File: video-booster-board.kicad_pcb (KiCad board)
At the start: 4 copper layers, 39 x 41.5 mm, 140 parts, among them IC1 INA180A1IDBVT, J1 0473460001, J10 M20-9990246, J11 MC-HVT1-S04-G, J12 solder_jumper, J13 solder_jumper, J14 solder_jumper, J2 CHDMI-AMSS-01-C-Vertical, J3 CHDMI-AMSS-01-C-Vertical, J4 694103107102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

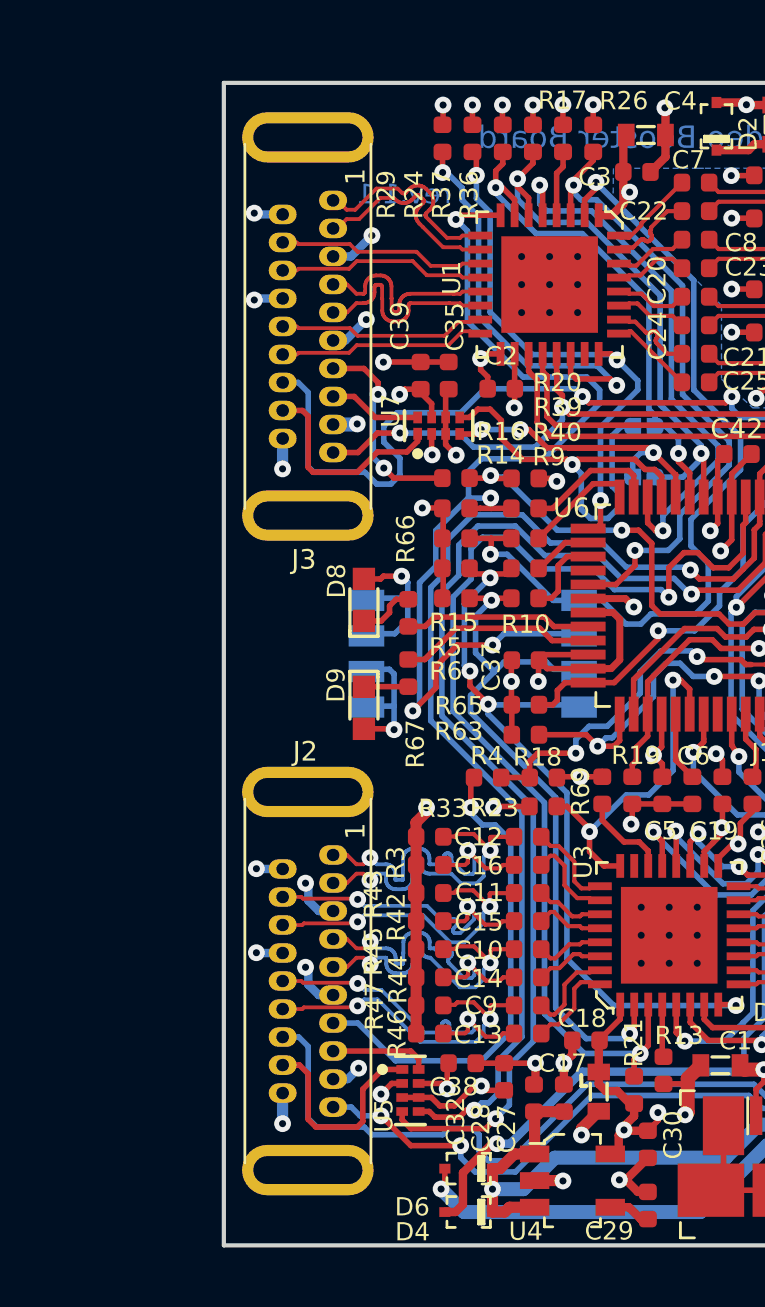
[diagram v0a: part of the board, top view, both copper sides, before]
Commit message: Restored plating on HDMI angular connectors
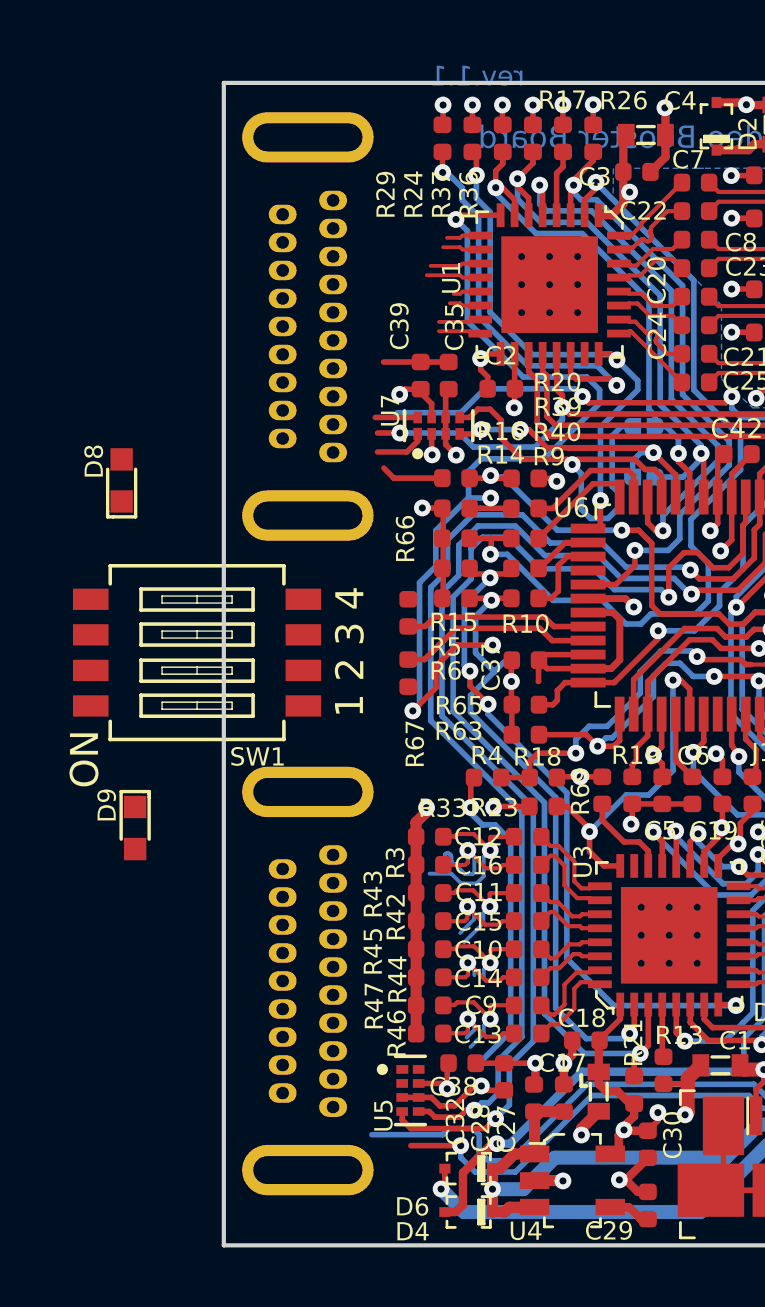
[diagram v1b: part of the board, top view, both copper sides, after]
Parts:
- J2, J3: moved to B.Cu
- SW1: value 1571983-5 -> VAL**; moved to F.Cu
- moved SW1 9.84 mm to (110.0, 78.8), turned to 90 degrees
- moved D8 9.64 mm to (107.4, 72.7)
- moved D9 9.22 mm to (107.8, 85.1)
- turned J2 to 270 degrees
- turned J3 to 270 degrees
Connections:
- J2 pad 12: GND -> /TX_IN_CLK_N
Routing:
- net GND: track 107.7 -> 82.7 mm, vias 58 -> 44
- net /RX_UTILITY: track 34.7 -> 24.6 mm
- net /TX_IN_D0_P: track 12.3 -> 4.21 mm, vias 2 -> 1
- net /TX_IN_D0_N: track 12.1 -> 4.09 mm, vias 2 -> 1
- net /TX_IN_CLK_P: track 12.5 -> 4.63 mm, vias 2 -> 1
- net /TX_SRC_SDA: track 7.66 -> 0.00 mm
- net /TX_IN_CLK_N: track 12.2 -> 4.77 mm, vias 2 -> 1
- net /TX_IN_D1_P: track 12.0 -> 4.66 mm, vias 2 -> 1
- net /TX_IN_D1_N: track 12.3 -> 5.24 mm, vias 2 -> 1
- net /RX_OUT_D0_P: track 7.45 -> 0.98 mm
- net /RX_OUT_D0_N: track 7.45 -> 1.12 mm
- net /TX_IN_D2_P: track 12.2 -> 5.90 mm, vias 2 -> 1
- net /RX_OUT_D2_P: track 7.44 -> 1.22 mm
- net /TX_UTILITY: track 36.8 -> 30.7 mm
- net Net-(J2-Pad13): track 17.6 -> 11.4 mm
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
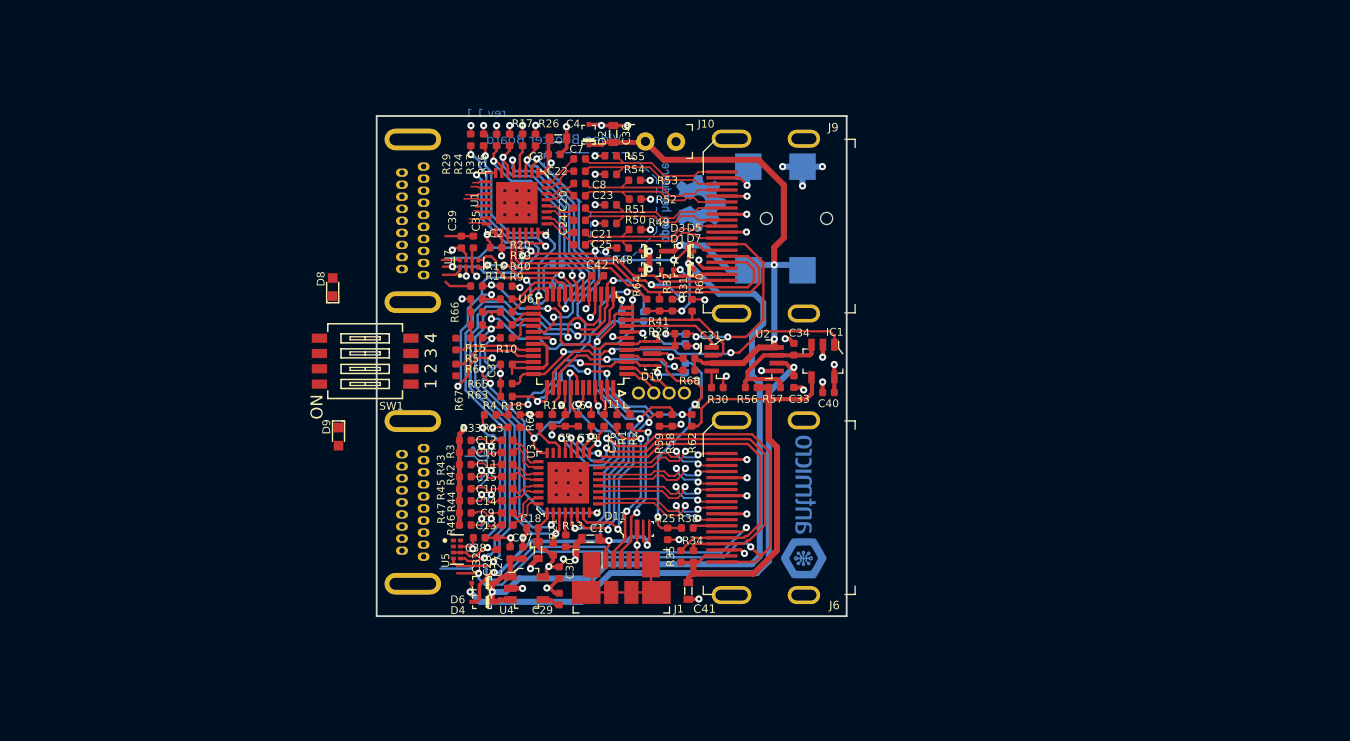
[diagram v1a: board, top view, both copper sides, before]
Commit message: Changed TX/RX side of PCB layout
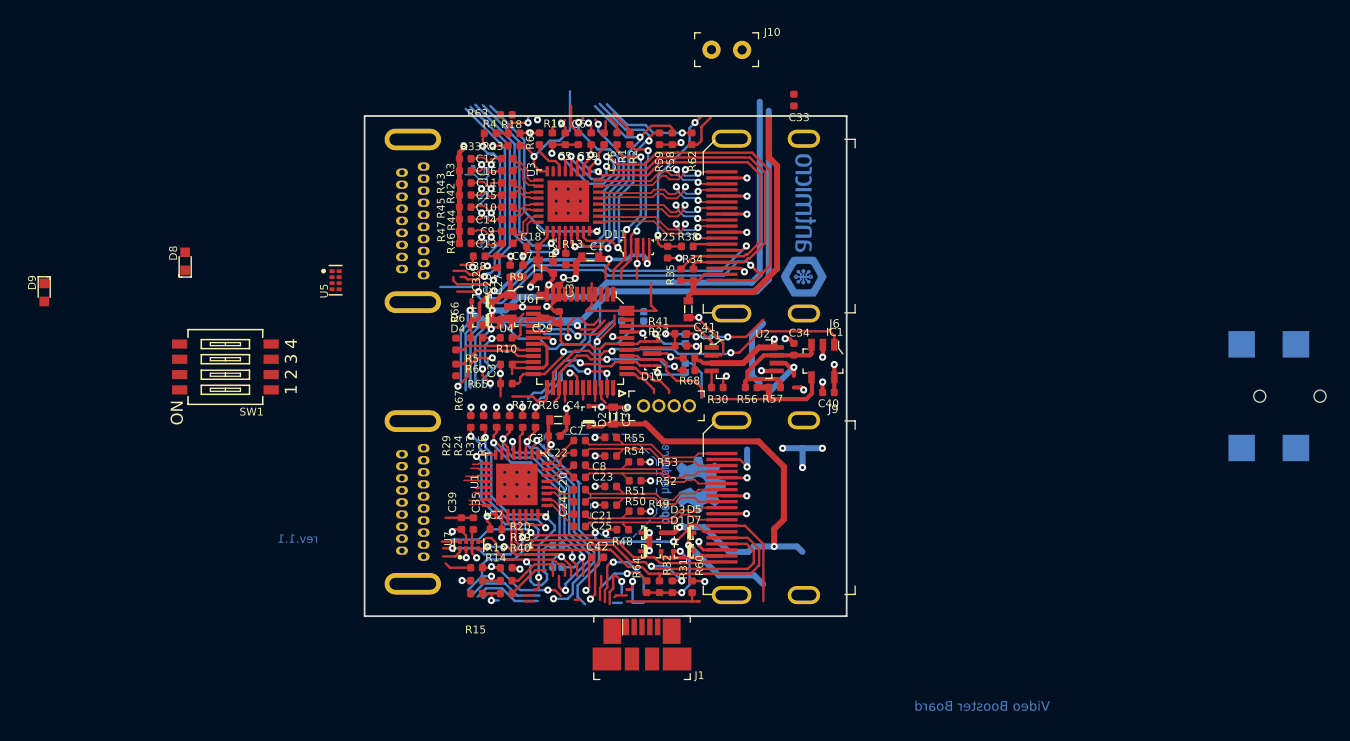
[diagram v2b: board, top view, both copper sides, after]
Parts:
- moved J4 43.5 mm to (190.8, 81.7)
- moved D9 27.2 mm to (83.4, 73.1)
- moved U5 24.5 mm to (107.6, 72.1)
- moved C11 23.4 mm to (121.8, 64.1)
- moved C15 23.4 mm to (121.8, 65.1)
- moved C16 23.4 mm to (121.8, 63.0)
- moved C17 23.4 mm to (124.4, 71.1)
- moved C18 23.4 mm to (123.9, 69.3)
- moved C20 23.4 mm to (127.8, 89.5)
- moved C21 23.4 mm to (127.8, 91.5)
- moved C22 23.4 mm to (127.8, 86.4)
- moved C25 23.4 mm to (127.8, 92.6)
- moved C27 23.4 mm to (123.1, 71.4)
- moved C28 23.4 mm to (122.1, 71.4)
- moved C32 23.4 mm to (121.0, 70.6)
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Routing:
- net /TX_DDET: track 39.5 -> 31.1 mm, vias 2 -> 1
- net +5V: track 62.0 -> 68.7 mm, vias 2 -> 3
- net +5VA: track 52.7 -> 46.6 mm
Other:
- board size 39 x 41.5 mm -> 40 x 41.5 mm

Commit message: Routing in progress
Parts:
- moved J10 51.7 mm to (134.7, 104.5)
- moved J1 44.1 mm to (132.6, 59.5), turned to 0 degrees
- moved C33 35.1 mm to (111.0, 62.9)
- moved C26 34.0 mm to (102.3, 80.3)
- moved D11 31.2 mm to (102.0, 63.4)
- moved C1 30.8 mm to (157.1, 82.1)
- moved C36 27.3 mm to (157.1, 90.2)
- moved U4 26.3 mm to (100.2, 86.5)
- moved D2 24.8 mm to (153.3, 85.4)
- moved R63 24.0 mm to (99.9, 68.5)
- moved R9 23.0 mm to (98.8, 73.9)
- moved R2 22.8 mm to (130.8, 83.1)
- moved R1 22.8 mm to (129.9, 83.1)
- moved C5 22.5 mm to (126.6, 82.9)
- moved C6 22.5 mm to (127.7, 82.9)
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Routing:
- net +5V: track 68.7 -> 2.96 mm, vias 3 -> 0
- net /TX_SRC_SCL_3V: track 45.6 -> 2.03 mm, vias 3 -> 1
- net /TX_SRC_SDA_3V: track 43.6 -> 2.96 mm, vias 3 -> 1
- net /VUSB: track 39.6 -> 1.11 mm, vias 4 -> 0
- net /RX_EQ0: track 33.7 -> 1.49 mm, vias 4 -> 0
- net +5VA: track 46.6 -> 19.3 mm, vias 3 -> 2
- net /TX_HPD: track 64.1 -> 39.0 mm, vias 4 -> 3
- net GND: track 82.7 -> 58.3 mm, vias 44 -> 33
- net /TX_UTILITY: track 30.7 -> 53.7 mm, vias 1 -> 2
- net /TX_SINK_SCL_3V: track 31.7 -> 9.69 mm, vias 3 -> 1
- net /TX_SRC_5V: track 48.8 -> 26.9 mm, vias 3 -> 1
- net /TX_IN_CLK_P: track 4.63 -> 25.4 mm
- net /TX_IN_D1_N: track 5.24 -> 25.8 mm
- net /TX_DDET: track 31.1 -> 11.0 mm, vias 1 -> 2
- net /TX_SINK_SDA_3V: track 32.9 -> 13.2 mm, vias 3 -> 2
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
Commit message: Routing II
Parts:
- SW1: value VAL** -> 1571983-5
- moved C1 28.8 mm to (128.4, 84.3)
- moved R9 23.0 mm to (121.8, 73.9)
- moved C4 20.2 mm to (105.9, 85.7)
- moved R39 18.1 mm to (122.3, 79.0), turned to 90 degrees
- moved R5 18.0 mm to (120.8, 76.9), turned to 180 degrees
- moved R10 17.8 mm to (121.8, 74.8)
- moved R14 17.7 mm to (120.8, 79.5), turned to 180 degrees
- moved R15 17.5 mm to (120.8, 80.7), turned to 180 degrees
- moved U7 17.3 mm to (117.8, 86.0)
- moved R40 16.5 mm to (120.8, 81.7)
- moved R6 16.0 mm to (120.8, 78.2), turned to 180 degrees
- moved J8 12.5 mm to (122.1, 84.1), turned to 180 degrees
- moved J12 11.5 mm to (120.4, 84.1), turned to 180 degrees
- moved R29 11.4 mm to (122.8, 72.9), turned to 0 degrees
- moved U5 11.3 mm to (118.8, 73.8), turned to 90 degrees
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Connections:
- J2 pad 11: (no net) -> GND
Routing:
- net /TX_HIZ_EN: track 3.99 -> 32.2 mm, vias 0 -> 2
- net /RX_EQ0: track 1.49 -> 13.2 mm, vias 0 -> 2
- net /RX_HIZ_EN: track 19.2 -> 29.5 mm, vias 3 -> 2
- net /RX_SINK_SDA_3V: track 9.31 -> 19.6 mm, vias 1 -> 3
- net /RX_EQ1_R: track 3.58 -> 13.3 mm, vias 0 -> 2
- net /RX_DCC_EN: track 14.9 -> 6.04 mm
- net /RX_SINK_CEC: track 14.5 -> 7.78 mm, vias 3 -> 1
- net GND: track 58.3 -> 64.7 mm, vias 33 -> 38
- net /RX_SINK_SCL_3V: track 11.2 -> 17.3 mm, vias 1 -> 3
- net /RX_UTILITY: track 22.4 -> 17.2 mm, vias 3 -> 2
- net /RX_SRC_SCL_3V: track 17.9 -> 22.8 mm
- net /TX_EQ1: track 11.4 -> 16.4 mm, vias 1 -> 3
- net /ADC5: track 5.15 -> 0.28 mm, vias 1 -> 0
- net /TX_EQ0: track 16.2 -> 20.8 mm, vias 1 -> 3
- net /TX_HPD_3V: track 13.2 -> 17.4 mm, vias 1 -> 2
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
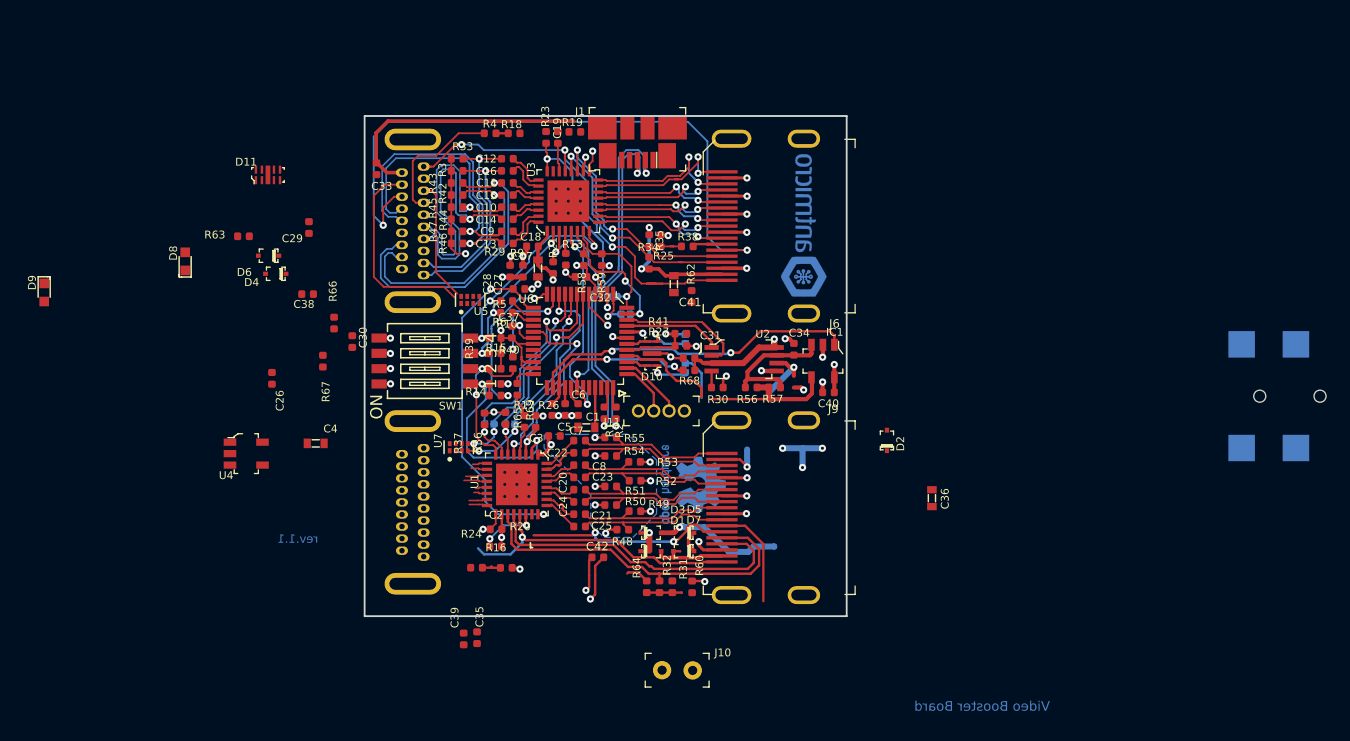
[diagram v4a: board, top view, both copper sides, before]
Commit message: SWD changed from pinhead to testpads, routing in progress
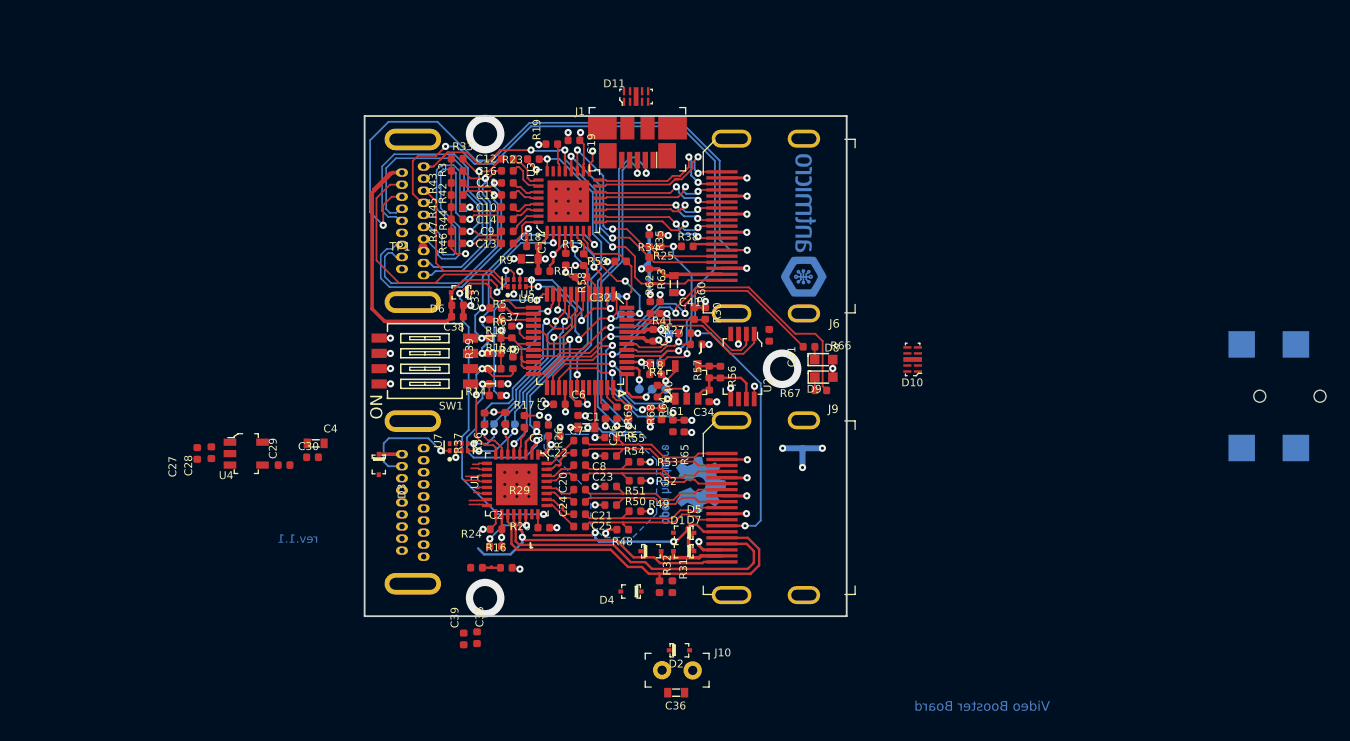
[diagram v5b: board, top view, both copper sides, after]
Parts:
- removed J11: MC-HVT1-S04-G, video-booster-board-footprints:PinHeader_1x4_P1.27mm_Drill.7mm
- added TP1: TP_SMD_0_75MM, antmicro-footprints:Testpoint_smd_0_75mm, F.Cu at (114.8, 69.4)
- added TP2: TP_SMD_0_75MM, antmicro-footprints:Testpoint_smd_0_75mm, B.Cu at (135.0, 81.1)
- added TP3: TP_SMD_0_75MM, antmicro-footprints:Testpoint_smd_0_75mm, B.Cu at (132.8, 81.1)
- added TP4: TP_SMD_0_75MM, antmicro-footprints:Testpoint_smd_0_75mm, B.Cu at (133.9, 81.1)
- moved D9 65.1 mm to (148.1, 80.2), turned to 0 degrees
- moved D8 53.6 mm to (148.1, 78.7), turned to 0 degrees
- moved R67 41.4 mm to (147.9, 81.3), turned to 180 degrees
- moved D4 39.5 mm to (132.1, 98.0)
- moved R66 39.5 mm to (146.9, 77.6), turned to 0 degrees
- moved R63 35.1 mm to (134.5, 74.4), turned to 270 degrees
- moved D11 31.2 mm to (132.5, 56.9)
- moved C27 31.0 mm to (96.1, 86.5)
- moved C28 29.0 mm to (97.3, 86.4)
- moved C26 27.8 mm to (130.0, 83.1)
- moved C36 26.7 mm to (135.9, 106.3), turned to 0 degrees
- moved D2 24.5 mm to (136.1, 102.8), turned to 0 degrees
- moved R4 23.5 mm to (134.2, 79.0), turned to 180 degrees
- moved D3 23.3 mm to (111.2, 87.4), turned to 270 degrees
- moved R18 23.2 mm to (134.1, 79.9)
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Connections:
- J1 pad SH: Net-(J1-PadSH) -> GND
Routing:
- net Net-(J2-Pad13): track 11.3 -> 52.0 mm, vias 0 -> 2
- net /DBG_LED_TX: track 0.00 -> 33.1 mm, vias 0 -> 2
- net /DBG_LED_RX: track 0.00 -> 27.4 mm, vias 0 -> 2
- net +5VA: track 19.3 -> 1.92 mm
- net /ADC4: track 4.08 -> 19.8 mm, vias 0 -> 3
- net /ADC5: track 0.28 -> 14.5 mm, vias 0 -> 2
- net Net-(J9-Pad13): track 8.80 -> 22.3 mm, vias 0 -> 2
- net /ADC6: track 27.2 -> 14.1 mm
- net /TX_SRC_5V: track 26.9 -> 39.4 mm, vias 1 -> 2
- net /TX_SRC_SDA_3V: track 3.20 -> 14.2 mm, vias 1 -> 3
- net /TX_SRC_SCL_3V: track 2.03 -> 11.8 mm, vias 1 -> 3
- net /RX_SINK_SDA: track 0.00 -> 9.27 mm, vias 0 -> 1
- net /TX_HIZ_EN: track 32.2 -> 24.0 mm
- net /TX_SINK_5V: track 24.6 -> 18.1 mm, vias 2 -> 3
- net /VUSB: track 3.32 -> 9.09 mm, vias 0 -> 1
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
